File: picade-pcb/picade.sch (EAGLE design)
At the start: 55 parts

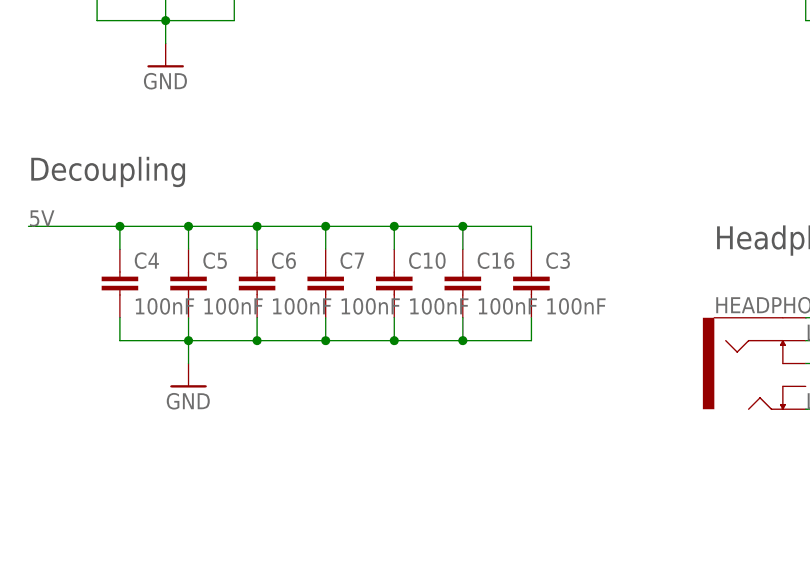
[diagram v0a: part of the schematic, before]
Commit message: Moved vias and stuff to avoid new silk
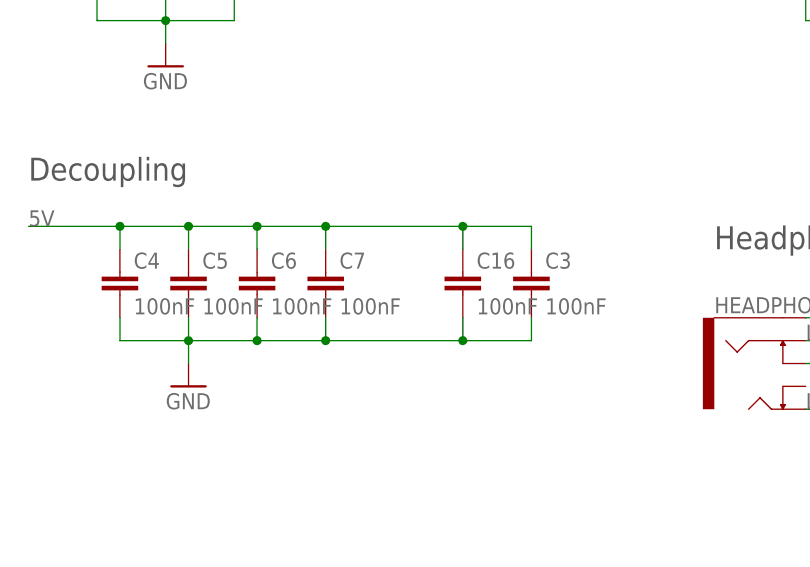
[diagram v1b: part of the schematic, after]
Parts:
- removed C10: 100nF, resistor:C-EUC0603K
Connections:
- net 5V: no longer C10.1
- net GND: no longer C10.2
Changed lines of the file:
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@@
 <part name="GND6" library="supply1" deviceset="GND" device=""/>
 <part name="C7" library="resistor" deviceset="C-EU" device="C0603K" value="100nF"/>
-<part name="C10" library="resistor" deviceset="C-EU" device="C0603K" value="100nF"/>
 <part name="BL" library="adafruit" deviceset="LED" device="CHIPLED_0805"/>
 <part name="GND2" library="supply1" deviceset="GND" device=""/>
@@
 <instance part="GND6" gate="1" x="12.7" y="40.64"/>
 <instance part="C7" gate="G$1" x="154.94" y="48.26"/>
-<instance part="C10" gate="G$1" x="162.56" y="48.26"/>
 <instance part="BL" gate="G$1" x="38.1" y="114.3" rot="R90"/>
 <instance part="GND2" gate="1" x="45.72" y="109.22"/>
@@
 <wire x1="154.94" y1="40.64" x2="154.94" y2="43.18" width="0.1524" layer="91"/>
 <junction x="147.32" y="40.64"/>
-<pinref part="C10" gate="G$1" pin="2"/>
-<wire x1="154.94" y1="40.64" x2="162.56" y2="40.64" width="0.1524" layer="91"/>
-<wire x1="162.56" y1="40.64" x2="162.56" y2="43.18" width="0.1524" layer="91"/>
 <junction x="154.94" y="40.64"/>
-<junction x="162.56" y="40.64"/>
 <pinref part="C16" gate="G$1" pin="2"/>
-<wire x1="162.56" y1="40.64" x2="170.18" y2="40.64" width="0.1524" layer="91"/>
+<wire x1="154.94" y1="40.64" x2="170.18" y2="40.64" width="0.1524" layer="91"/>
 <wire x1="170.18" y1="40.64" x2="170.18" y2="43.18" width="0.1524" layer="91"/>
 <wire x1="170.18" y1="40.64" x2="177.8" y2="40.64" width="0.1524" layer="91"/>
@@
 <wire x1="147.32" y1="53.34" x2="154.94" y2="53.34" width="0.1524" layer="91"/>
 <junction x="147.32" y="53.34"/>
-<pinref part="C10" gate="G$1" pin="1"/>
-<wire x1="154.94" y1="53.34" x2="162.56" y2="53.34" width="0.1524" layer="91"/>
-<wire x1="162.56" y1="53.34" x2="162.56" y2="50.8" width="0.1524" layer="91"/>
 <pinref part="C7" gate="G$1" pin="1"/>
 <wire x1="154.94" y1="53.34" x2="154.94" y2="50.8" width="0.1524" layer="91"/>
 <junction x="154.94" y="53.34"/>
 <pinref part="C16" gate="G$1" pin="1"/>
-<wire x1="162.56" y1="53.34" x2="170.18" y2="53.34" width="0.1524" layer="91"/>
+<wire x1="154.94" y1="53.34" x2="170.18" y2="53.34" width="0.1524" layer="91"/>
 <wire x1="170.18" y1="53.34" x2="170.18" y2="50.8" width="0.1524" layer="91"/>
-<junction x="162.56" y="53.34"/>
 <wire x1="170.18" y1="53.34" x2="177.8" y2="53.34" width="0.1524" layer="91"/>
 <junction x="170.18" y="53.34"/>
